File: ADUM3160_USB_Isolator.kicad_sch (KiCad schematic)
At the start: 22 parts, among them J1 USB_A, J2 USB_A, J3 Conn_01x03_Pin, J4 Conn_01x03_Pin, U1 ADUM3160

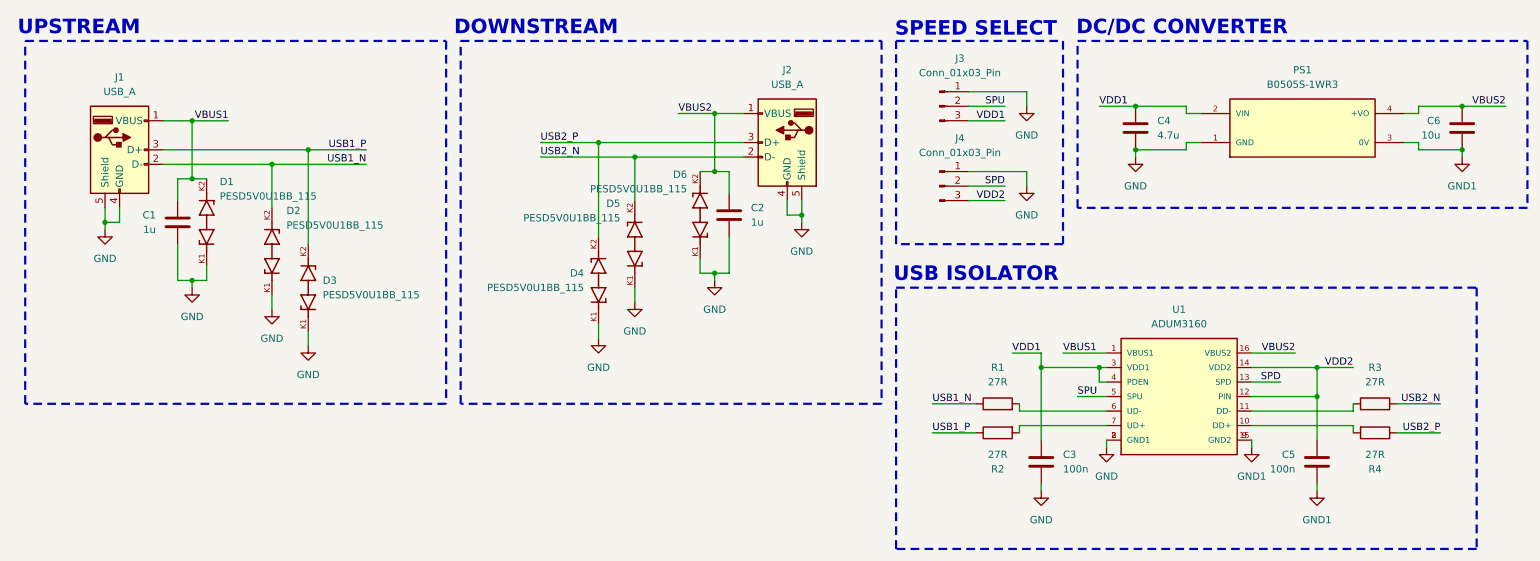
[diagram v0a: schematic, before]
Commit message: Footprint Update
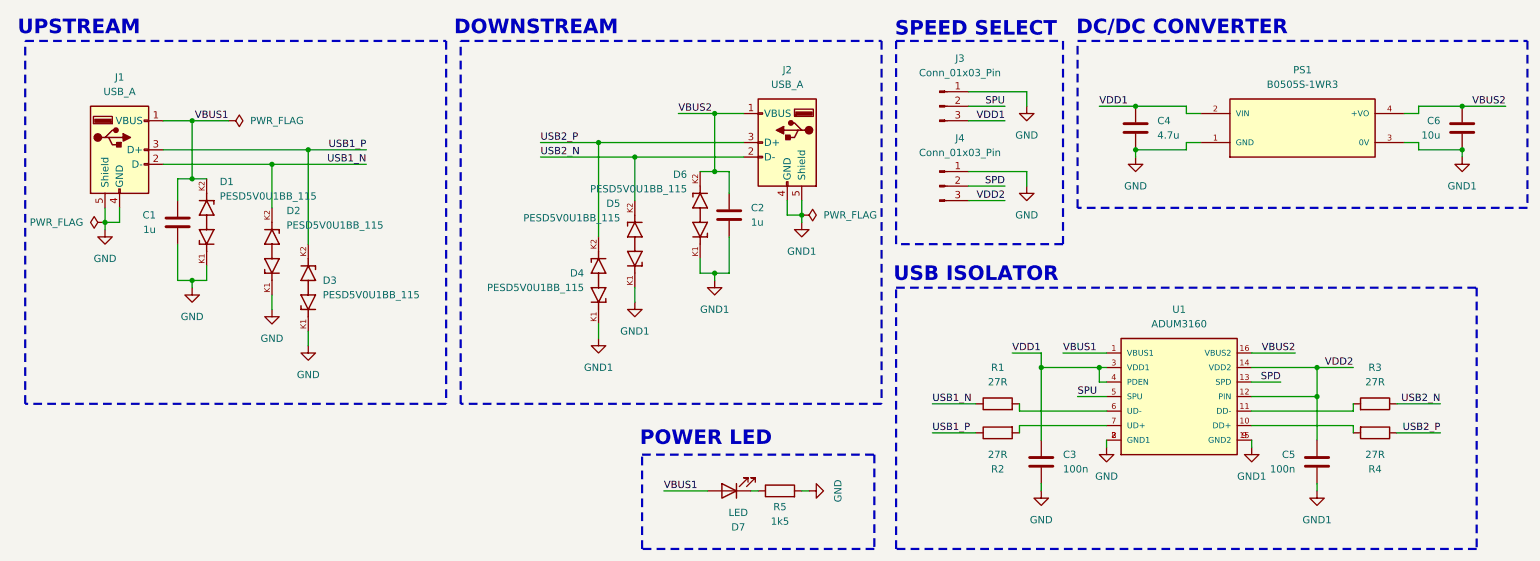
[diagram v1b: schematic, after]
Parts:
- added D7: LED, LED_SMD:LED_0603_1608Metric_Pad1.05x0.95mm_HandSolder, symbol Device:LED
- added R5: 1k5, Resistor_SMD:R_0603_1608Metric_Pad0.98x0.95mm_HandSolder, symbol Device:R
- C1, C2, C3, C4, C5, C6: footprint (none) -> Capacitor_SMD:C_0603_1608Metric_Pad1.08x0.95mm_HandSolder
- J1: footprint (none) -> KSZ_KiCad_Footprint_Library:SAMTEC_USB-AM-S-X-X-TH
- J2: footprint (none) -> Connector_USB:USB_A_Molex_67643_Horizontal
- J3, J4: footprint (none) -> Connector_PinHeader_2.54mm:PinHeader_1x03_P2.54mm_Vertical
- R1, R2, R3, R4: footprint (none) -> Resistor_SMD:R_0603_1608Metric_Pad0.98x0.95mm_HandSolder
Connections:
- net GND: now also R5.2; no longer C2.1, D4.K1, D5.K1, D6.K1, J2.4 (GND), J2.5 (Shield)
- net GND1: now also C2.1, D4.K1, D5.K1, D6.K1, J2.4 (GND), J2.5 (Shield)
- net VBUS1: now also D7.2 (A)
- new net: D7.1 (K), R5.1
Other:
- note added: "POWER LED"

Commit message: PCB & Layout update
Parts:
- removed J1: USB_A, KSZ_KiCad_Footprint_Library:SAMTEC_USB-AM-S-X-X-TH, symbol Connector:USB_A
- added J1: USB-AM-S-X-X-TH, KSZ_KiCad_Footprint_Library:SAMTEC_USB-AM-S-X-X-TH, symbol KSZ_KiCad_Symbol_Library:USB-AM-S-X-X-TH
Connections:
- net GND: now also J1.04 (GND), J1.S1 (SHIELD), J1.S2 (SHIELD); no longer J4.1 (Pin_1)
- net GND1: now also J4.1 (Pin_1)
- net USB1_N: now also D3.K2, J1.02 (D-); no longer D2.K2
- net USB1_P: now also D2.K2, J1.03 (D+); no longer D3.K2
- net VBUS1: now also C4.2, PS1.2 (VIN), J1.01 (VCC)
- net VDD1: no longer C4.2, PS1.2 (VIN)
- net USB2_2N: now reaches R3.2, U1.11 (DD-)
- net USB2_2P: now reaches R4.2, U1.10 (DD+)
- net USB1_2N: now reaches R1.2, U1.6 (UD-)
- net USB1_2P: now reaches R2.2, U1.7 (UD+)
